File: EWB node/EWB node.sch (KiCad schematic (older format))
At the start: 30 parts, among them J1 USB_A, J2 Barrel_Jack_Switch, J3 AVR-ISP-6, J4 Conn_01x06, P1 USB_C_Plug_USB2.0, SW1 SW_Push_Dual, U1 USBLC6-2P6, U2 LP2985-3.3, U3 NCP1117-5.0_TO252, U4 ATmega328P-AU, Y1 16MHz

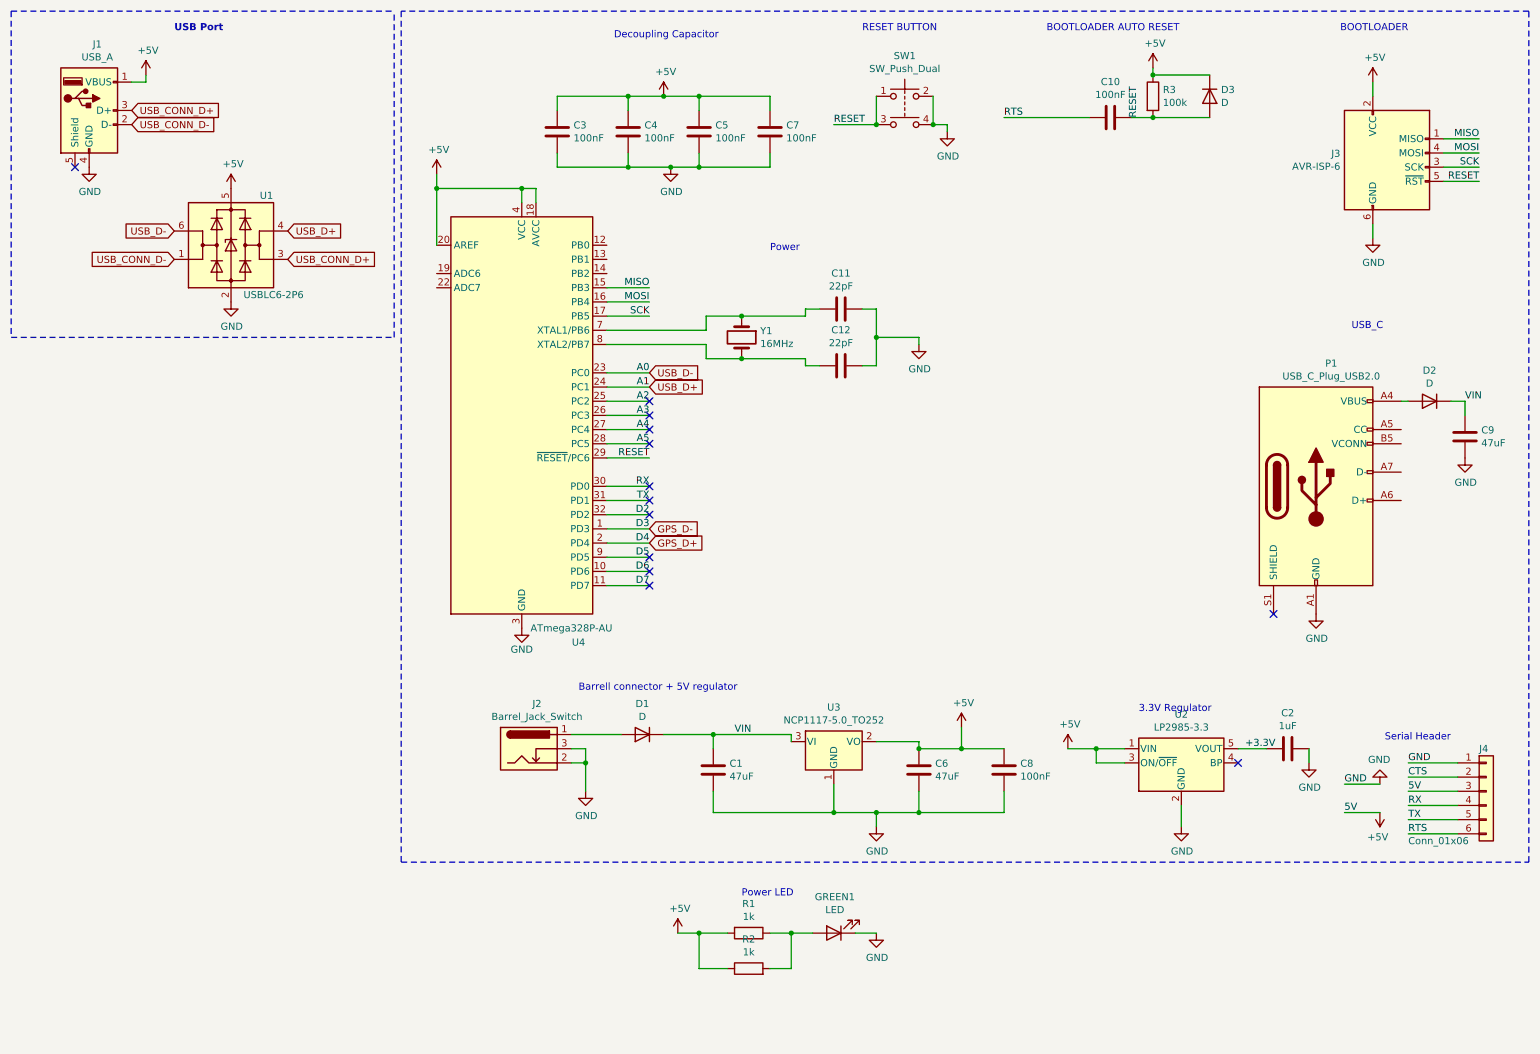
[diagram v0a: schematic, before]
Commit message: lora integration added
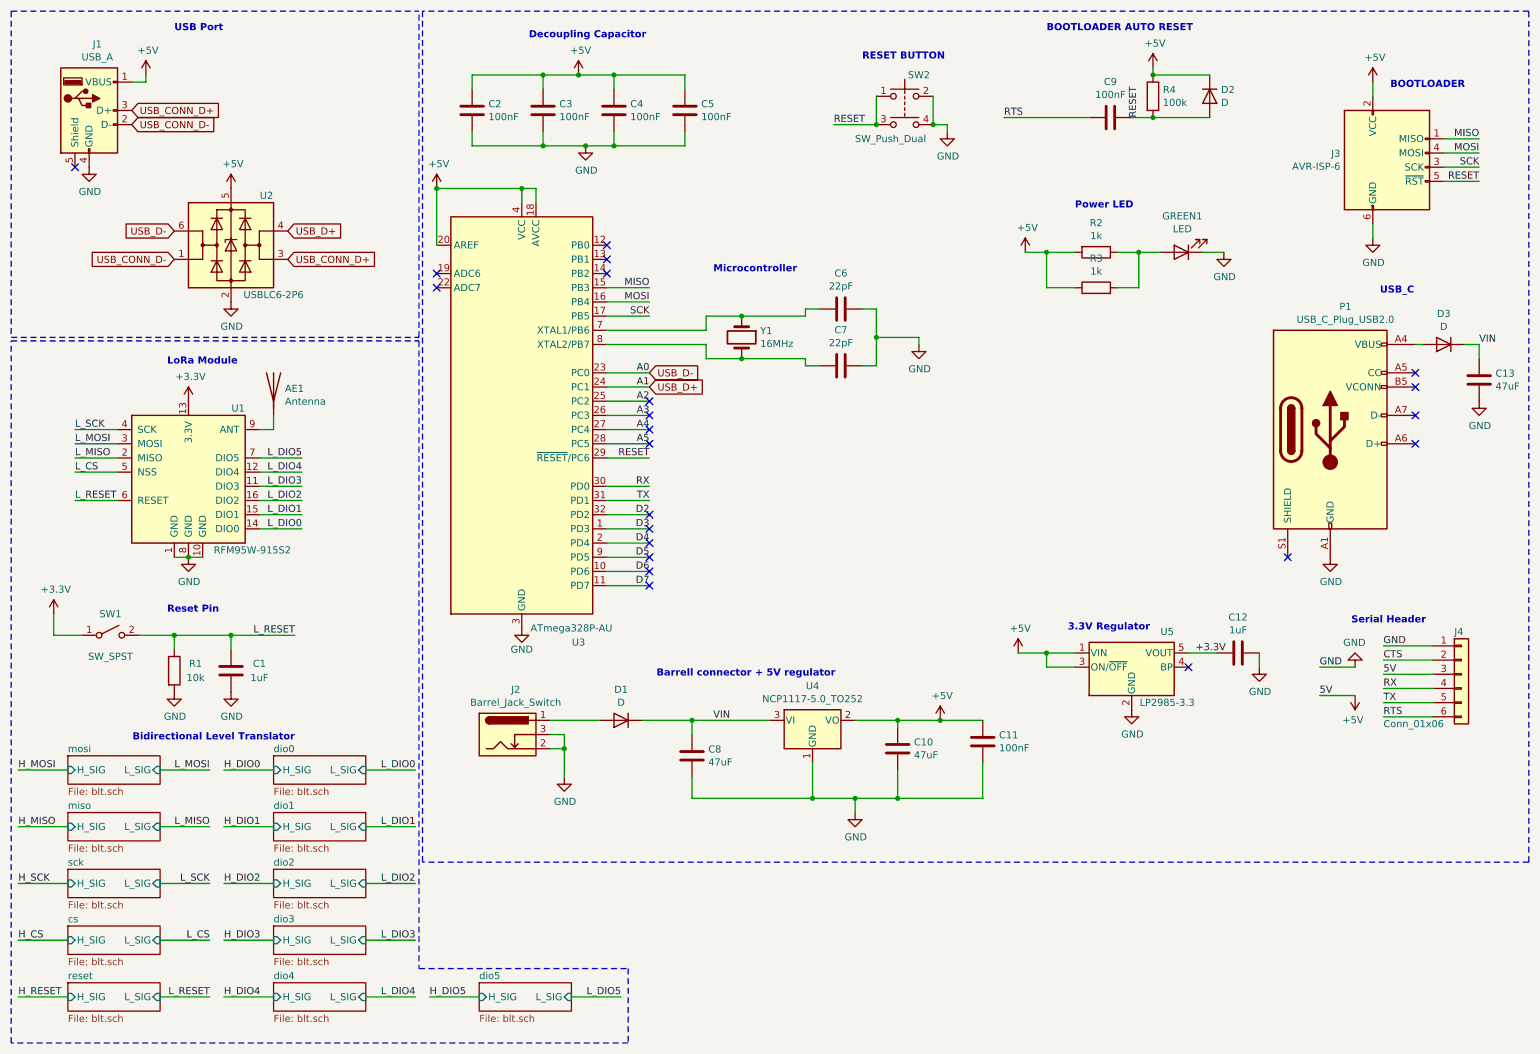
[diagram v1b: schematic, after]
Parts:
- added AE1: Antenna, symbol Device:Antenna
- added C1: 1uF, Capacitor_SMD:C_0201_0603Metric_Pad0.64x0.40mm_HandSolder, symbol Device:C
- added R1: 10k, Resistor_SMD:R_0603_1608Metric_Pad0.98x0.95mm_HandSolder, symbol Device:R
- added SW1: SW_SPST, symbol Switch:SW_SPST
- added U1: RFM95W-915S2, symbol RF_Module:RFM95W-915S2
- D1: footprint (none) -> Diode_SMD:D_0201_0603Metric_Pad0.64x0.40mm_HandSolder
- D2: renamed from D3; footprint (none) -> Diode_SMD:D_0201_0603Metric_Pad0.64x0.40mm_HandSolder
- D3: renamed from D2; footprint (none) -> Diode_SMD:D_0201_0603Metric_Pad0.64x0.40mm_HandSolder
- GREEN1: footprint (none) -> LED_SMD:LED_0603_1608Metric_Pad1.05x0.95mm_HandSolder
- renumbered C6 to C10, C8 to C11, C2 to C12, C9 to C13, C3 to C2, C4 to C3, C5 to C4, C7 to C5, C11 to C6, C12 to C7, C1 to C8, C10 to C9, R1 to R2, R2 to R3, R3 to R4, SW1 to SW2, U1 to U2, U4 to U3, U3 to U4, U2 to U5
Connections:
- net GND: now also C1.1, R1.2, U1.1 (GND), U1.10 (GND), U1.8 (GND)
- net GPS_D+ renamed D4
- net GPS_D- renamed D3
- new net: AE1.1 (A), U1.9 (ANT)
- new net +3V3: SW1.1 (A), U1.13 (3.3V)
- new net L_CS: U1.5 (NSS)
- new net L_DIO0: U1.14 (DIO0)
- new net L_DIO1: U1.15 (DIO1)
- new net L_DIO2: U1.16 (DIO2)
- new net L_DIO3: U1.11 (DIO3)
- new net L_DIO4: U1.12 (DIO4)
- new net L_DIO5: U1.7 (DIO5)
- new net L_MISO: U1.2 (MISO)
- new net L_MOSI: U1.3 (MOSI)
- new net L_RESET: C1.2, R1.1, SW1.2 (B), U1.6 (RESET)
- new net L_SCK: U1.4 (SCK)
- no-connect marks 13 -> 22
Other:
- note added: "Bidirectional Level Translator"
- note added: "LoRa Module"
- note added: "Microcontroller"
- note added: "Reset Pin"
- note removed: "Power"
- moved on the sheet: C10, C11, C12, C13, C2, C3, C4, C5, C8, D1, D3, GREEN1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

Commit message: pcb layout
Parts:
- removed AE1: Antenna, symbol Device:Antenna
- removed C13: 47uF, Capacitor_SMD:C_0201_0603Metric_Pad0.64x0.40mm_HandSolder, symbol Device:C
- removed D3: D, Diode_SMD:D_0201_0603Metric_Pad0.64x0.40mm_HandSolder, symbol Device:D
- removed P1: USB_C_Plug_USB2.0, symbol Connector:USB_C_Plug_USB2.0
- added E1: ANT-916-CHP-T, ant-916-chp-t:ant-916-chp-t, symbol ANT-916-CHP-T:ANT-916-CHP-T
- C1, C10, C11, C12, C2, C3, C4, C5, C6, C7, C8, C9: footprint Capacitor_SMD:C_0201_0603Metric_Pad0.64x0.40mm_HandSolder -> Capacitor_SMD:C_0603_1608Metric_Pad1.08x0.95mm_HandSolder
- J1: footprint (none) -> digikey-footprints:USB_A_Female_UE27AC54100
- J2: footprint (none) -> Connector_BarrelJack:BarrelJack_CUI_PJ-036AH-SMT_Horizontal
- J3, J4: footprint (none) -> Connector_PinHeader_2.54mm:PinHeader_1x06_P2.54mm_Vertical
- SW1: footprint (none) -> Button_Switch_SMD:SW_SPST_B3S-1000
- SW2: footprint (none) -> Button_Switch_SMD:SW_DIP_SPSTx02_Slide_6.7x6.64mm_W8.61mm_P2.54mm_LowProfile
- U1: footprint (none) -> RF_Module:HOPERF_RFM9XW_SMD
- Y1: footprint (none) -> Crystal:Crystal_SMD_0603-2Pin_6.0x3.5mm_HandSoldering
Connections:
- net at U1.9 (ANT): now also E1.1
- no-connect marks 22 -> 17
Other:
- note removed: "USB_C"
- moved on the sheet: C10, C11, C12, C8, D1, GREEN1, J2, J4, R2, R3, U4, U5
